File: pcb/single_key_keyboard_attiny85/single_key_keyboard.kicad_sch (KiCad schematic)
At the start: 22 parts, among them J1 USB_A, J4 Conn_01x04, J5 Conn_01x04, J6 Conn_01x04, J7 Conn_01x04, SW1 SW_Push, U1 ATtiny85-20P

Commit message: 3 boards version, stagger, missing led signals
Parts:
- R7: value 1k -> 47
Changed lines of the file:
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@@
 			)
 		)
-		(property "Value" "1k"
+		(property "Value" "47"
 			(at 146.304 53.34 90)
 			(effects

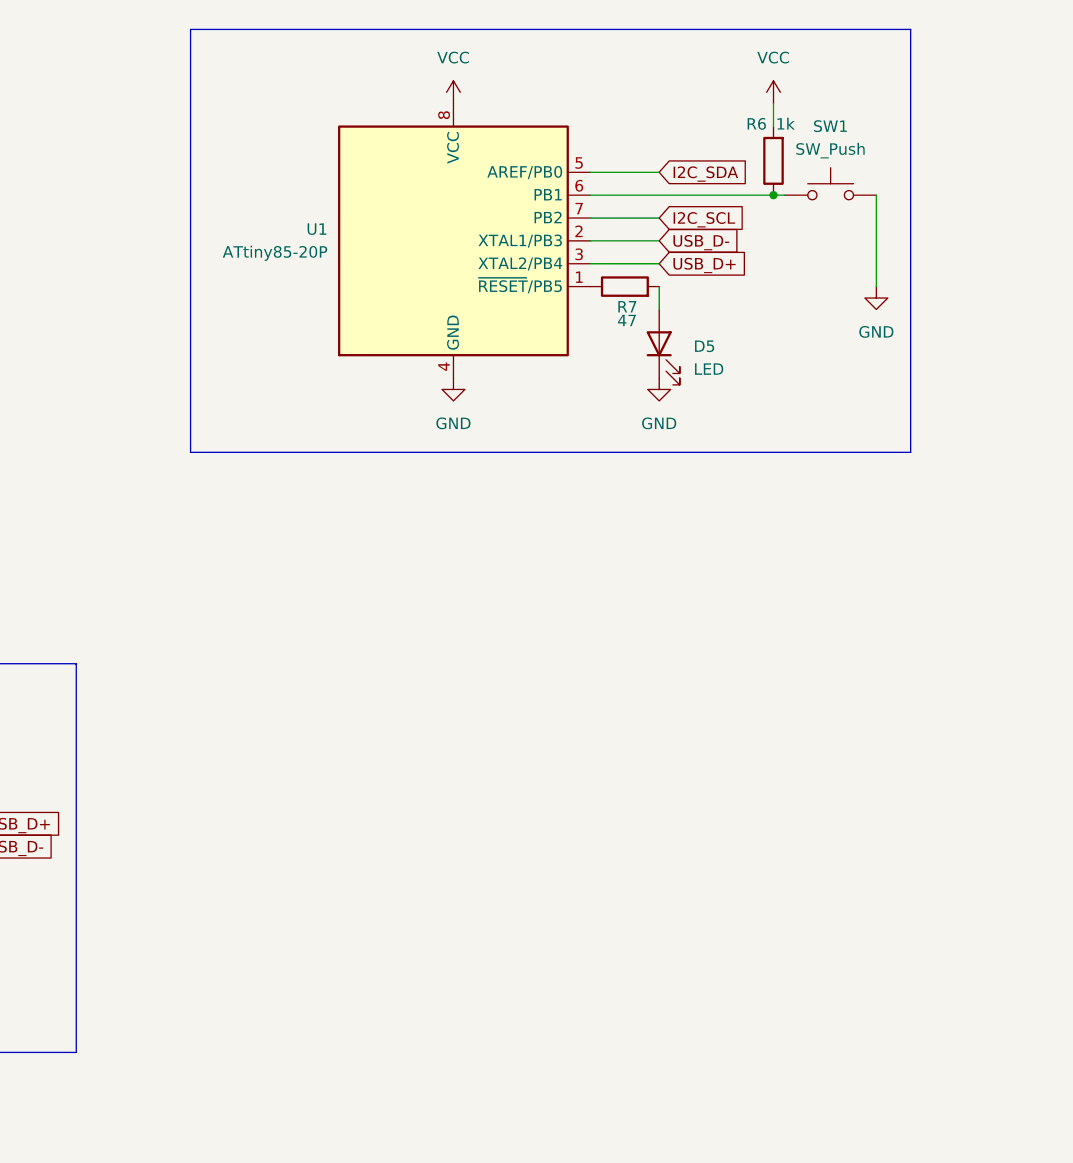
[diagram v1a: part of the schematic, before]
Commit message: swapped pins for button and led. Started designing the state machines
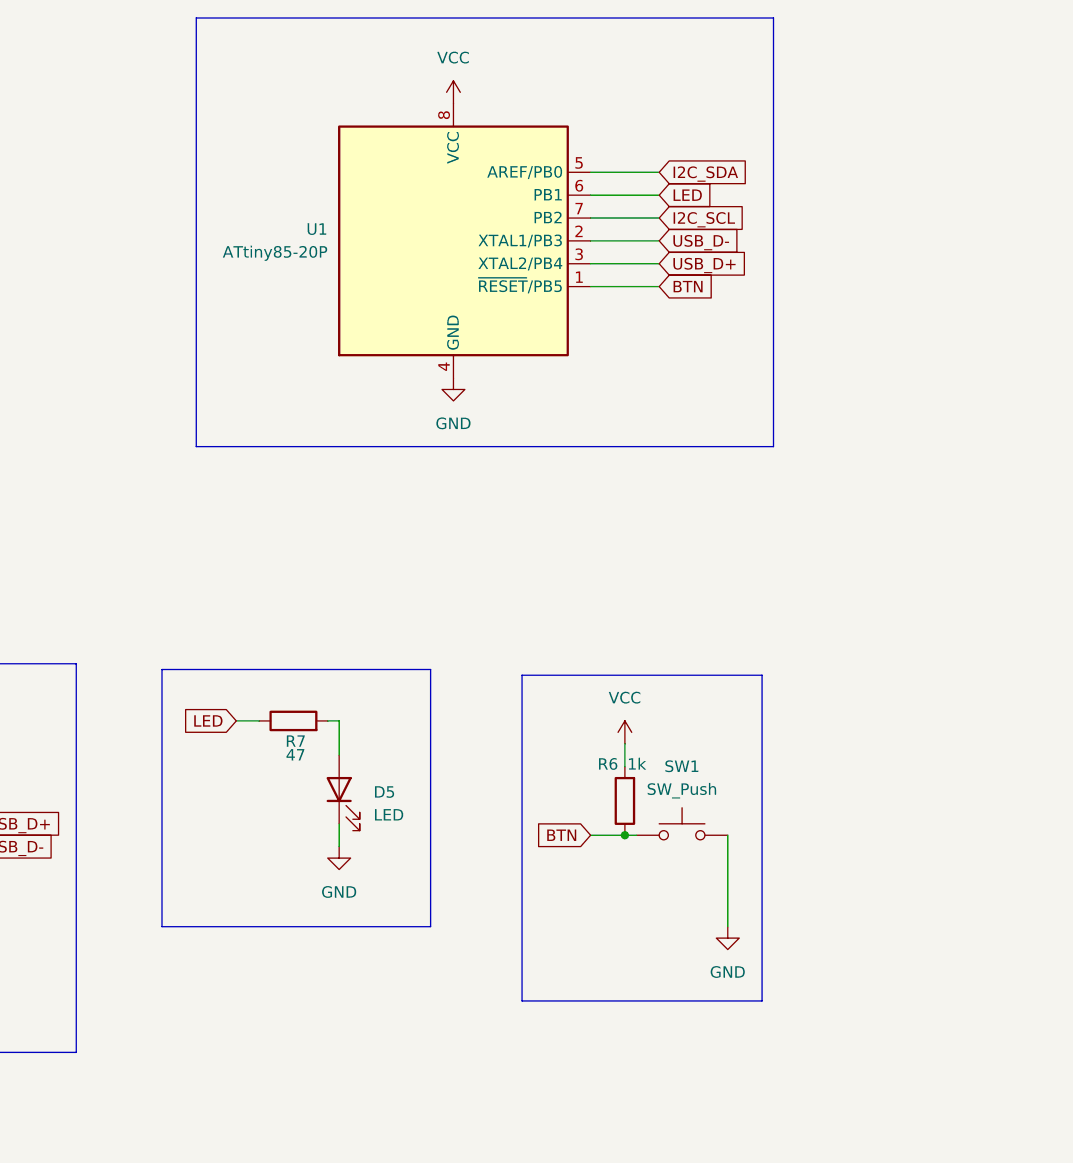
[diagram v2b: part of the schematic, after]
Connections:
- net BTN: now reaches U1.1 (~{RESET}/PB5)
- net BTN: now also R6.1, SW1.1; no longer R7.1
- new net LED: R7.1, U1.6 (PB1)
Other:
- moved on the sheet: D5, R6, R7, SW1
